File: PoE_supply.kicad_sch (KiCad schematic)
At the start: 24 parts, among them J1 Bus_RJ45_5-2337992-8, Q1 PJE138K, U1 TPS2372-3RGWR, U4 IEA48003A280V-001-R

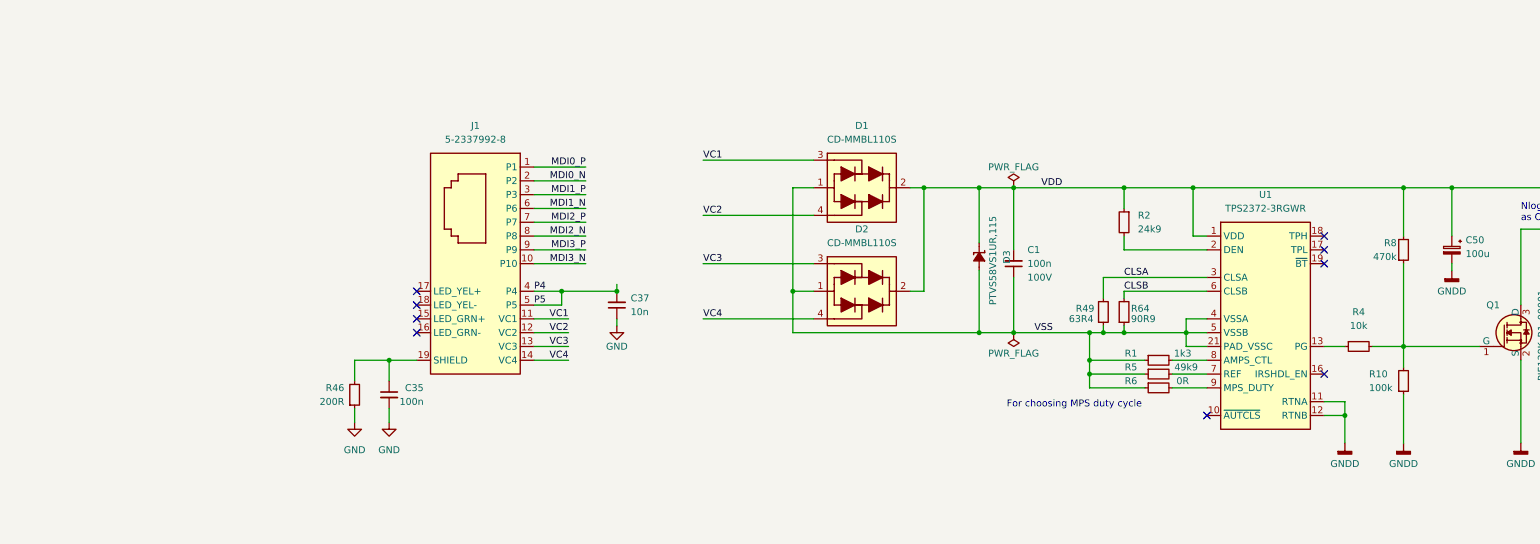
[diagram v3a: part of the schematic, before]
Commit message: [#62835] Add ETH receptacle diode steering
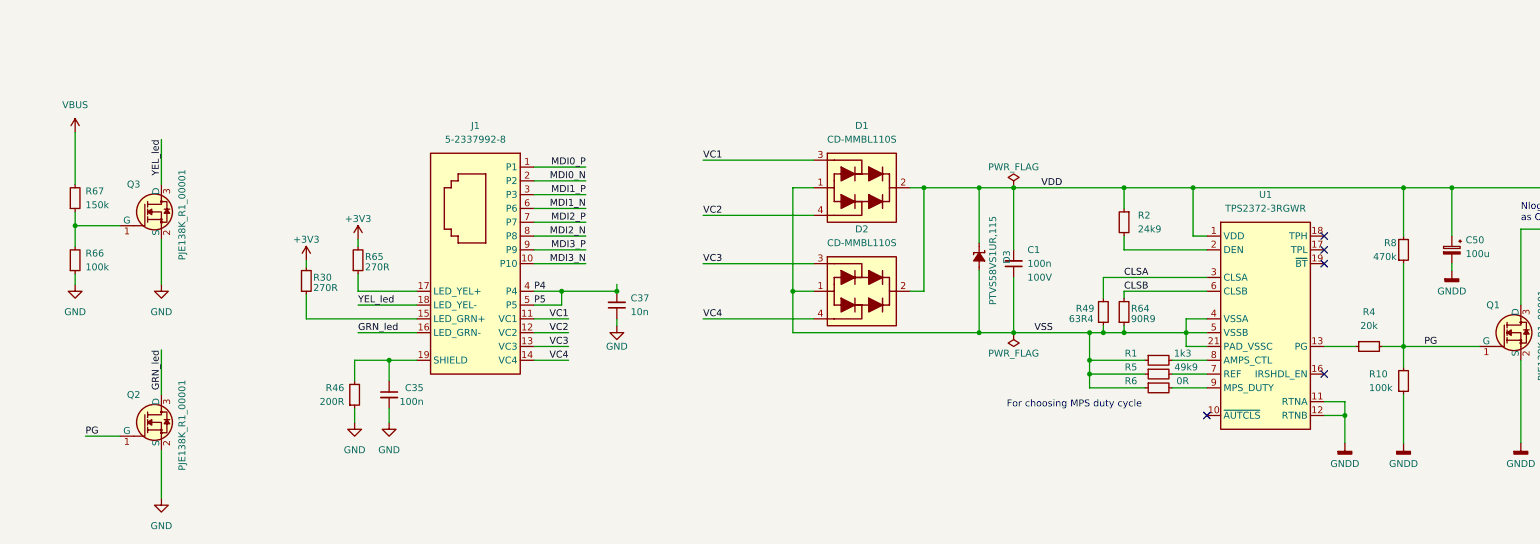
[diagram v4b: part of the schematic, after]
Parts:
- removed R4: R_10k_0402, antmicro-footprints:R_0402_1005Metric, symbol antmicroResistors0402:R_10k_0402
- added Q2, Q3: PJE138K, antmicro-footprints:SOT-523, symbol antmicroTransistorsFETsMOSFETsSingle:PJE138K
- added R30, R65: R_270R_0402, antmicro-footprints:R_0402_1005Metric, symbol antmicroResistors0402:R_270R_0402
- added R4: R_20k_0402, antmicro-footprints:R_0402_1005Metric, symbol antmicroResistors0402:R_20k_0402
- added R66: R_100k_0402, antmicro-footprints:R_0402_1005Metric, symbol antmicroResistors0402:R_100k_0402
- added R67: R_150k_0402, antmicro-footprints:R_0402_1005Metric, symbol antmicroResistors0402:R_150k_0402
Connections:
- net GND: now also Q2.2 (S), Q3.2 (S), R66.1
- net PG: now reaches Q1.1 (G), R10.2, R8.1
- net PG: now also Q2.1 (G), R4.2
- net at U1.13 (PG): now also R4.1
- net at J1.15 (LED_GRN+): now also R30.1
- net GRN_led: now reaches J1.16 (LED_GRN-)
- net GRN_led: now also Q2.3 (D)
- net at J1.17 (LED_YEL+): now also R65.1
- net YEL_led: now reaches J1.18 (LED_YEL-)
- net YEL_led: now also Q3.3 (D)
- new net: Q3.1 (G), R66.2, R67.1
- new net +3V3: R30.2, R65.2
- new net VBUS: R67.2
- no-connect marks 9 -> 5

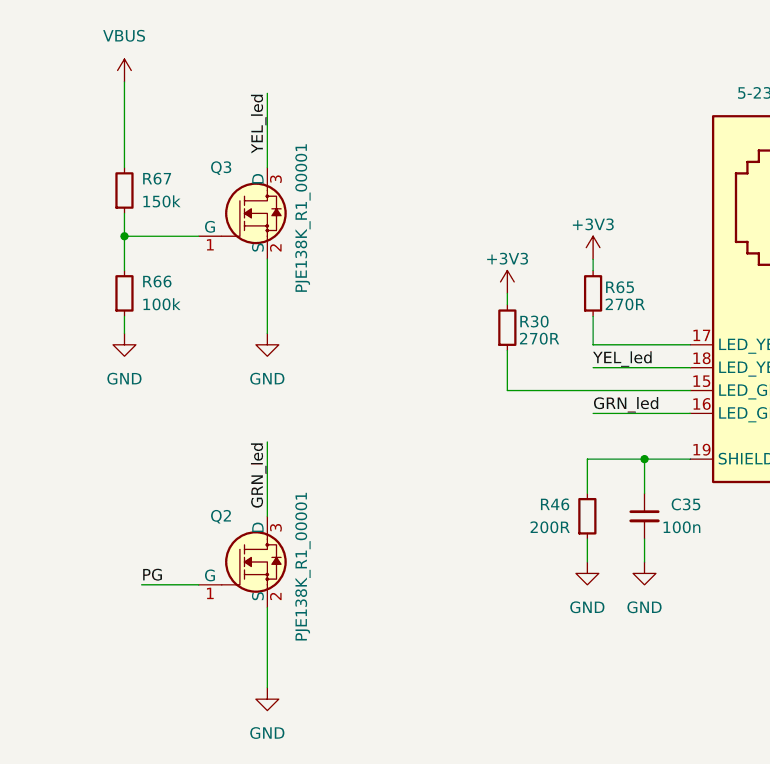
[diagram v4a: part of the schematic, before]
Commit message: [#62835] Add 3V3 LDO to PCB, place CBUS capacitors, change 5V buck layout
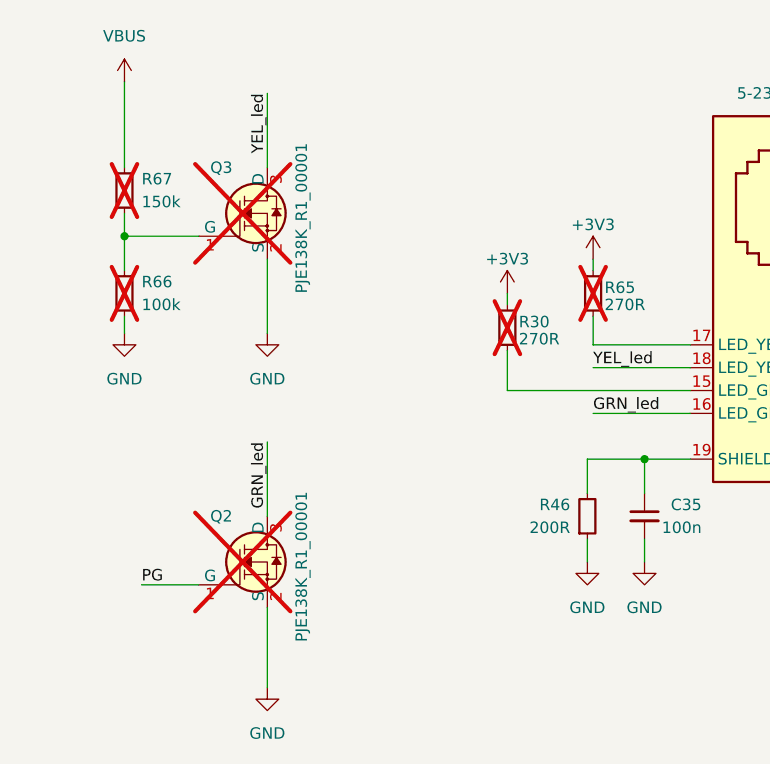
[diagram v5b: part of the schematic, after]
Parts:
- Q2, Q3, R30, R65, R66, R67: now not fitted
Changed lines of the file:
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@@
   )
   (symbol (lib_id "antmicroResistors0402:R_270R_0402") (at 75.565 123.825 90) (unit 1)
-    (in_bom yes) (on_board yes) (dnp no)
+    (in_bom yes) (on_board yes) (dnp yes)
     (property "Reference" "R65" (at 76.835 120.65 90)
       (effects (font (size 1.27 1.27) (thickness 0.15)) (justify right))
@@
   )
   (symbol (lib_name "PJE138K_2") (lib_id "antmicroTransistorsFETsMOSFETsSingle:PJE138K") (at 31.75 153.67 0) (unit 1)
-    (in_bom yes) (on_board yes) (dnp no)
+    (in_bom yes) (on_board yes) (dnp yes)
     (property "Reference" "Q2" (at 33.02 146.05 0)
       (effects (font (size 1.27 1.27) (thickness 0.15)) (justify left))
@@
   )
   (symbol (lib_id "antmicroResistors0402:R_150k_0402") (at 23.495 112.395 90) (unit 1)
-    (in_bom yes) (on_board yes) (dnp no) (fields_autoplaced)
+    (in_bom yes) (on_board yes) (dnp yes) (fields_autoplaced)
     (property "Reference" "R67" (at 25.4 108.585 90)
       (effects (font (size 1.27 1.27) (thickness 0.15)) (justify right))
@@
   )
   (symbol (lib_name "R_100k_0402_1") (lib_id "antmicroResistors0402:R_100k_0402") (at 23.495 123.825 90) (unit 1)
-    (in_bom yes) (on_board yes) (dnp no) (fields_autoplaced)
+    (in_bom yes) (on_board yes) (dnp yes) (fields_autoplaced)
     (property "Reference" "R66" (at 25.4 120.015 90)
       (effects (font (size 1.27 1.27) (thickness 0.15)) (justify right))
@@
   )
   (symbol (lib_name "PJE138K_2") (lib_id "antmicroTransistorsFETsMOSFETsSingle:PJE138K") (at 31.75 114.935 0) (unit 1)
-    (in_bom yes) (on_board yes) (dnp no)
+    (in_bom yes) (on_board yes) (dnp yes)
     (property "Reference" "Q3" (at 33.02 107.315 0)
       (effects (font (size 1.27 1.27) (thickness 0.15)) (justify left))
@@
   )
   (symbol (lib_id "antmicroResistors0402:R_270R_0402") (at 66.04 127.635 90) (unit 1)
-    (in_bom yes) (on_board yes) (dnp no)
+    (in_bom yes) (on_board yes) (dnp yes)
     (property "Reference" "R30" (at 67.31 124.46 90)
       (effects (font (size 1.27 1.27) (thickness 0.15)) (justify right))

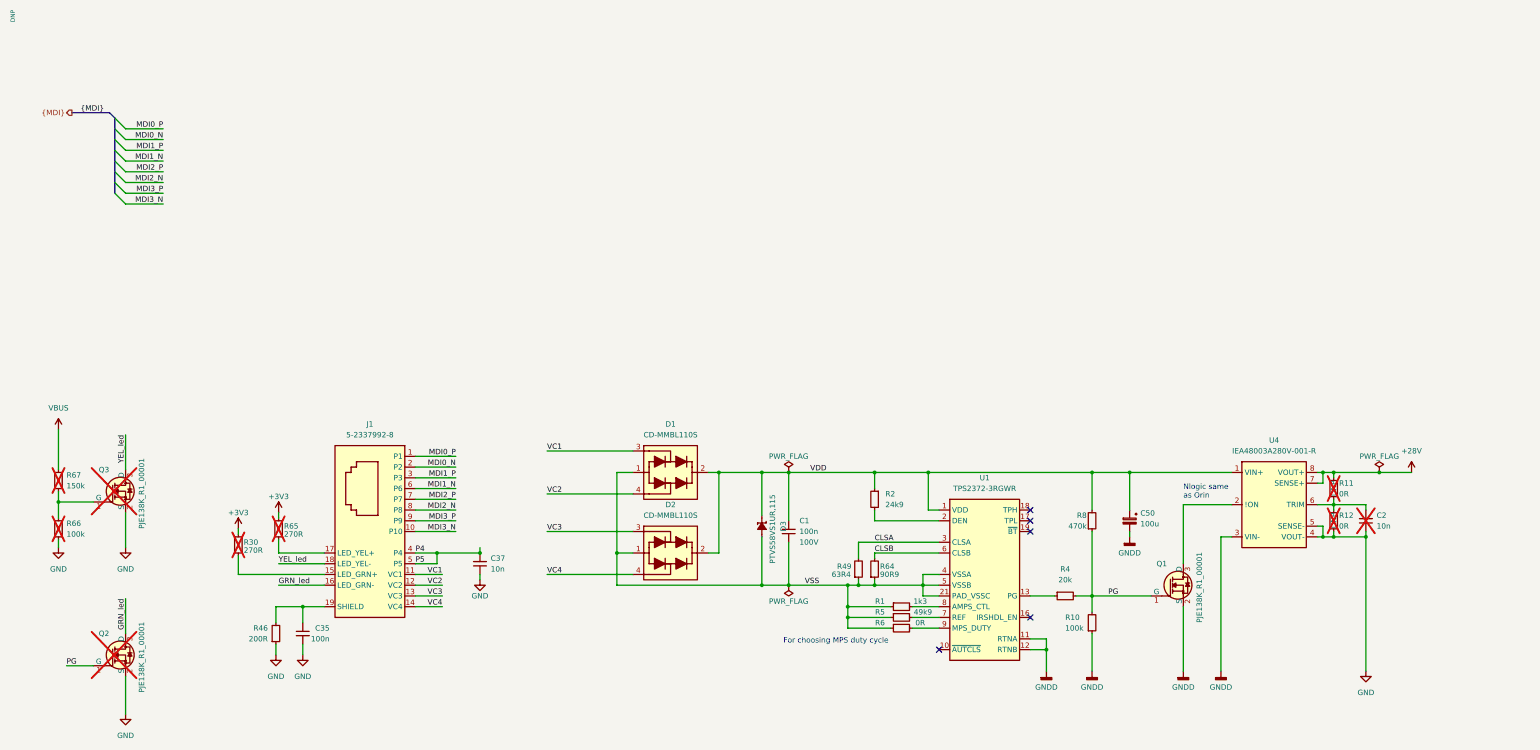
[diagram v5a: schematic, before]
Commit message: [#62835] Change IEA48003A280V-001-R input capacitors
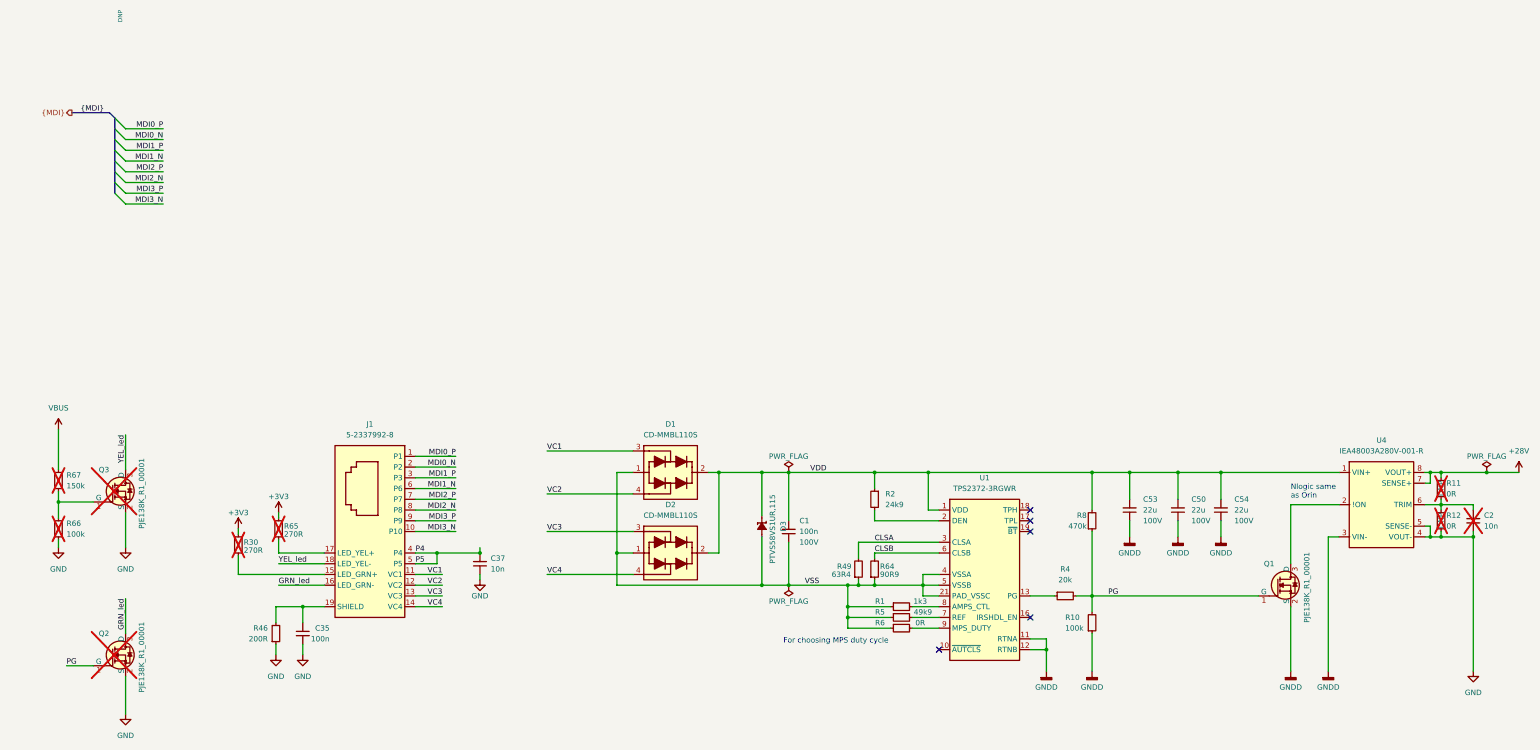
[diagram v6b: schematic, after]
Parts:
- removed C50: C_Pol_100u_100V_Vishay-150-CRZ-1213-D12.5mm-H13mm, antmicro-footprints:C_Pol_Vishay-1213-D12.5mm-H13mm, symbol antmicroCapacitorspol:C_Pol_100u_100V_Vishay-150-CRZ-1213-D12.5mm-H13mm
- added C50, C53, C54: C_22u_100V_2220, antmicro-footprints:C_2220_5650Metric, symbol antmicroCapacitorsmisc:C_22u_100V_2220
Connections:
- net GNDD: now also C50.1, C53.1, C54.1
- net VDD: now also C50.2, C53.2, C54.2
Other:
- moved on the sheet: C2, Q1, R11, R12, U4

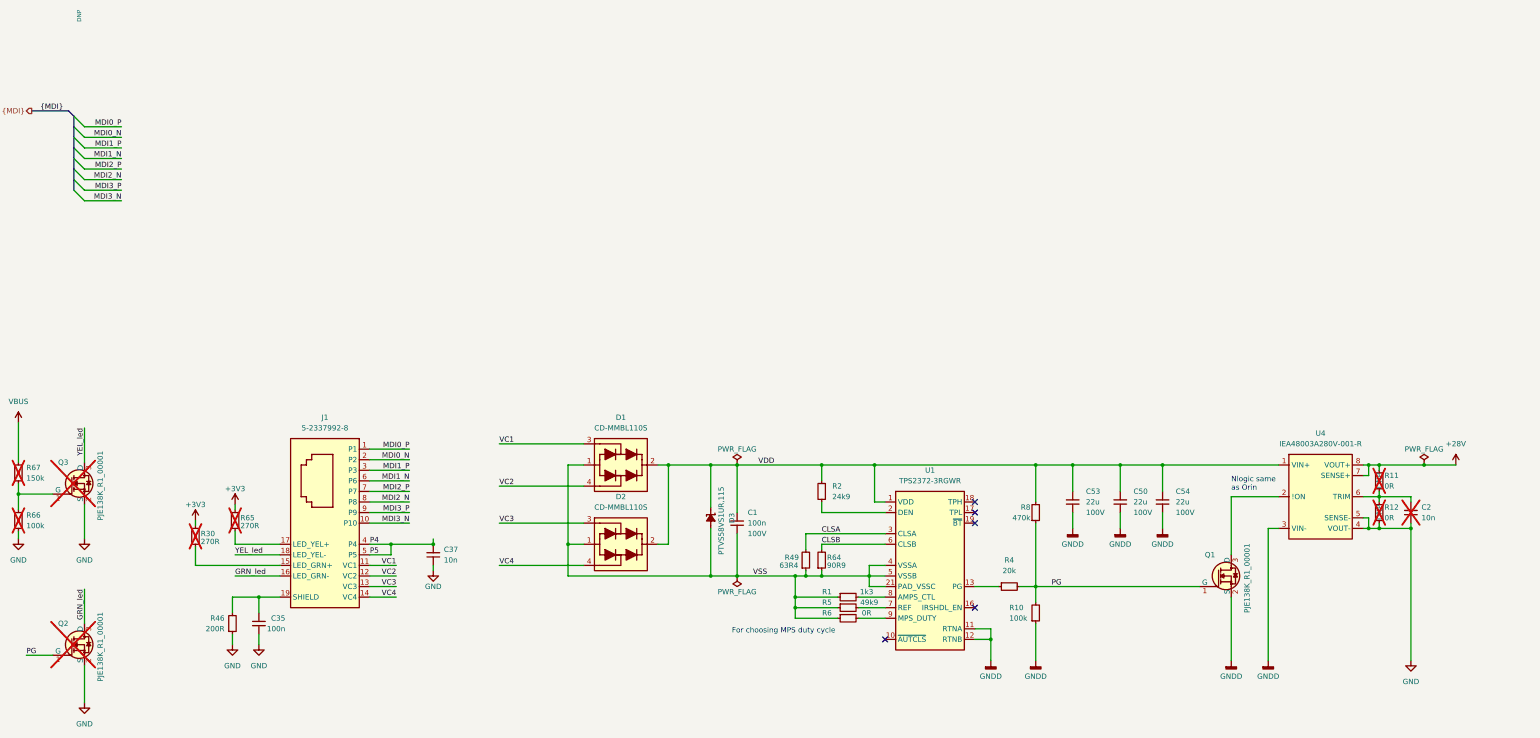
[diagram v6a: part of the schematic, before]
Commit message: [#63274] Add status LEDs for PoE controller
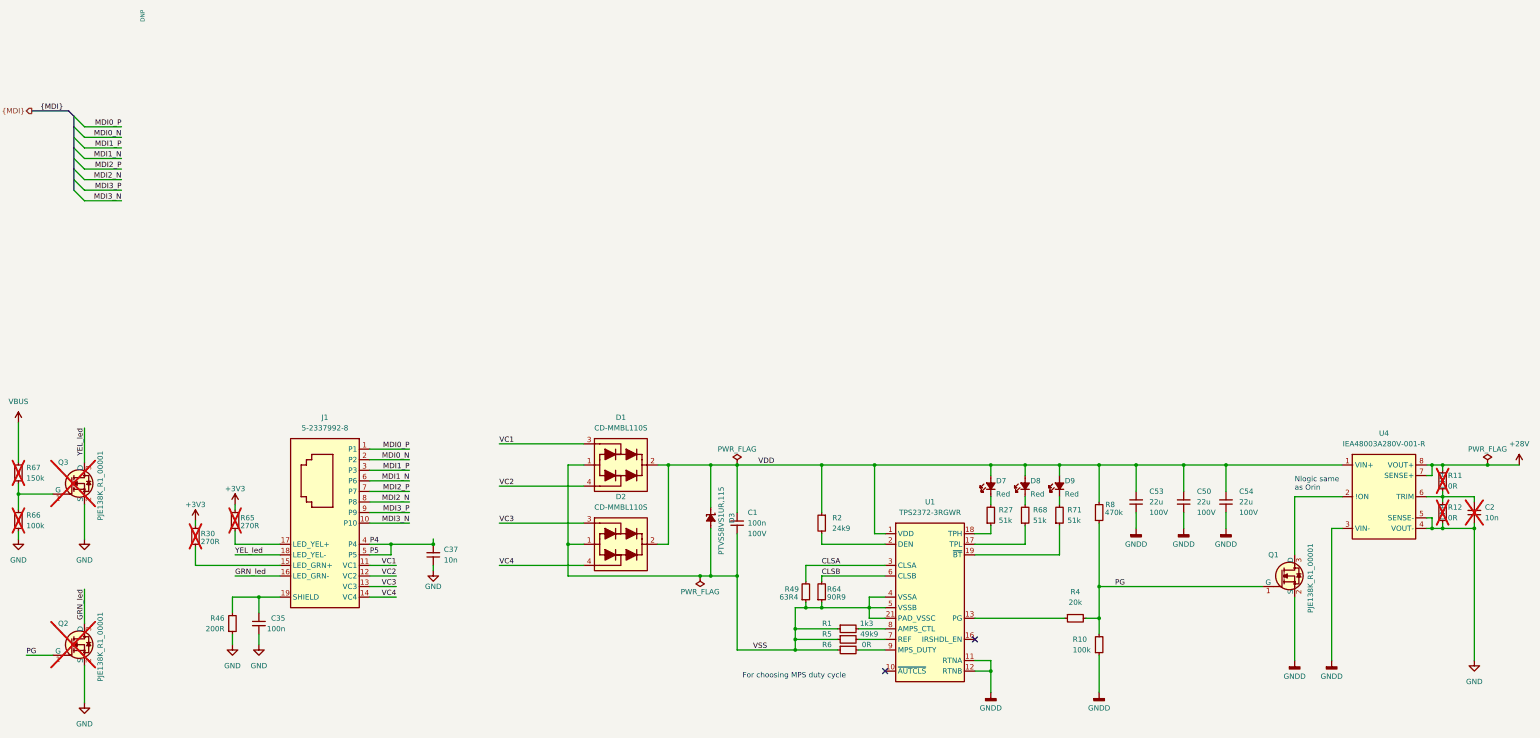
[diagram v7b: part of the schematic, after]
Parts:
- added D7, D8, D9: LED_R_0603_KP-1608EC, antmicro-footprints:LED_0603_1608Metric_R, symbol antmicroLEDIndicationDiscrete:LED_R_0603_KP-1608EC
- added R27, R68, R71: R_51k_0603, antmicro-footprints:R_0603_1608Metric, symbol antmicroResistors0603:R_51k_0603
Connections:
- net VDD: now also D7.2 (A), D8.2 (A), D9.2 (A)
- net at U1.17 (TPL): now also R68.1
- net at U1.18 (TPH): now also R27.1
- net at U1.19 (~{BT}): now also R71.1
- new net: D8.1 (C), R68.2
- new net: D7.1 (C), R27.2
- new net: D9.1 (C), R71.2
- no-connect marks 5 -> 2
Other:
- moved on the sheet: C2, C50, C53, C54, Q1, R1, R10, R11, R12, R2, R4, R49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

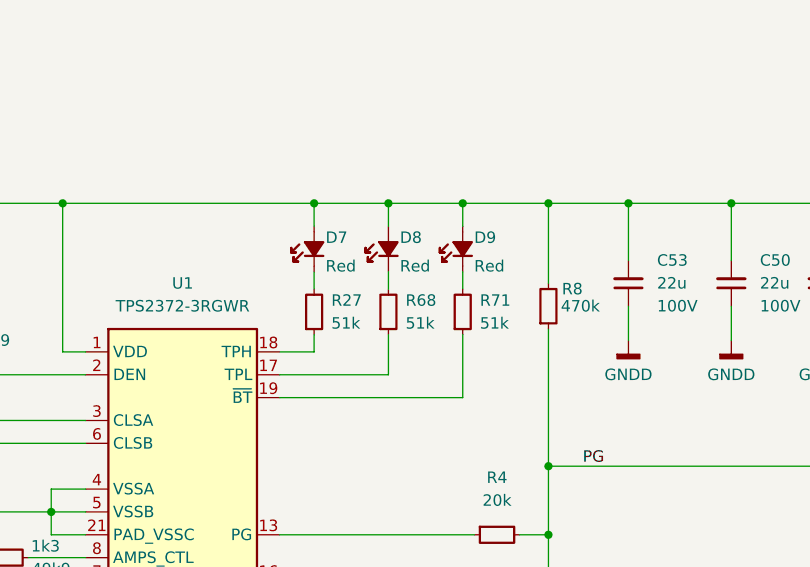
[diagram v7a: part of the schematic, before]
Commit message: [#63274] Add PSE type marking
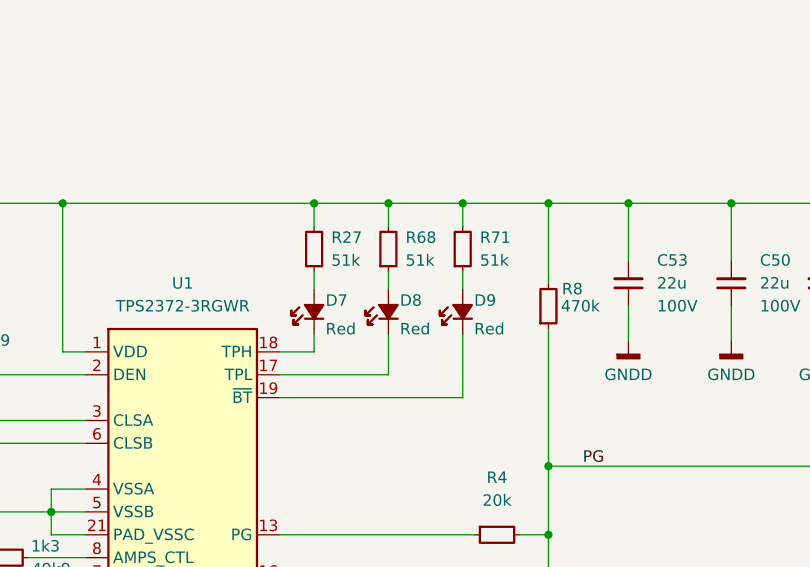
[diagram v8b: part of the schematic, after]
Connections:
- net VDD: now also R27.2, R68.2, R71.2; no longer D7.2 (A), D8.2 (A), D9.2 (A)
- net at R68.1: now also D8.2 (A); no longer U1.17 (TPL)
- net at D8.1 (C): now also U1.17 (TPL); no longer R68.2
- net at D7.1 (C): now also U1.18 (TPH); no longer R27.2
- net at D9.1 (C): now also U1.19 (~{BT}); no longer R71.2
- net at R27.1: now also D7.2 (A); no longer U1.18 (TPH)
- net at R71.1: now also D9.2 (A); no longer U1.19 (~{BT})
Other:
- moved on the sheet: D7, D8, D9, R27, R68, R71
